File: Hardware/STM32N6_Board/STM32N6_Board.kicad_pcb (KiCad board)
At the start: 4 copper layers, 82 x 78.7 mm, 148 parts, among them J1 Conn_01x02_Pin, J10 BOOT0, J11 Conn_01x18_Socket, J12 Conn_01x18_Socket, J2 Conn_01x02_Pin, J3 Conn_01x08_Pin, J4 Conn_01x18_Pin, J5 Conn_01x18_Pin, J6 Conn_01x05_Pin, J7 SFW15R-2STE1LF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

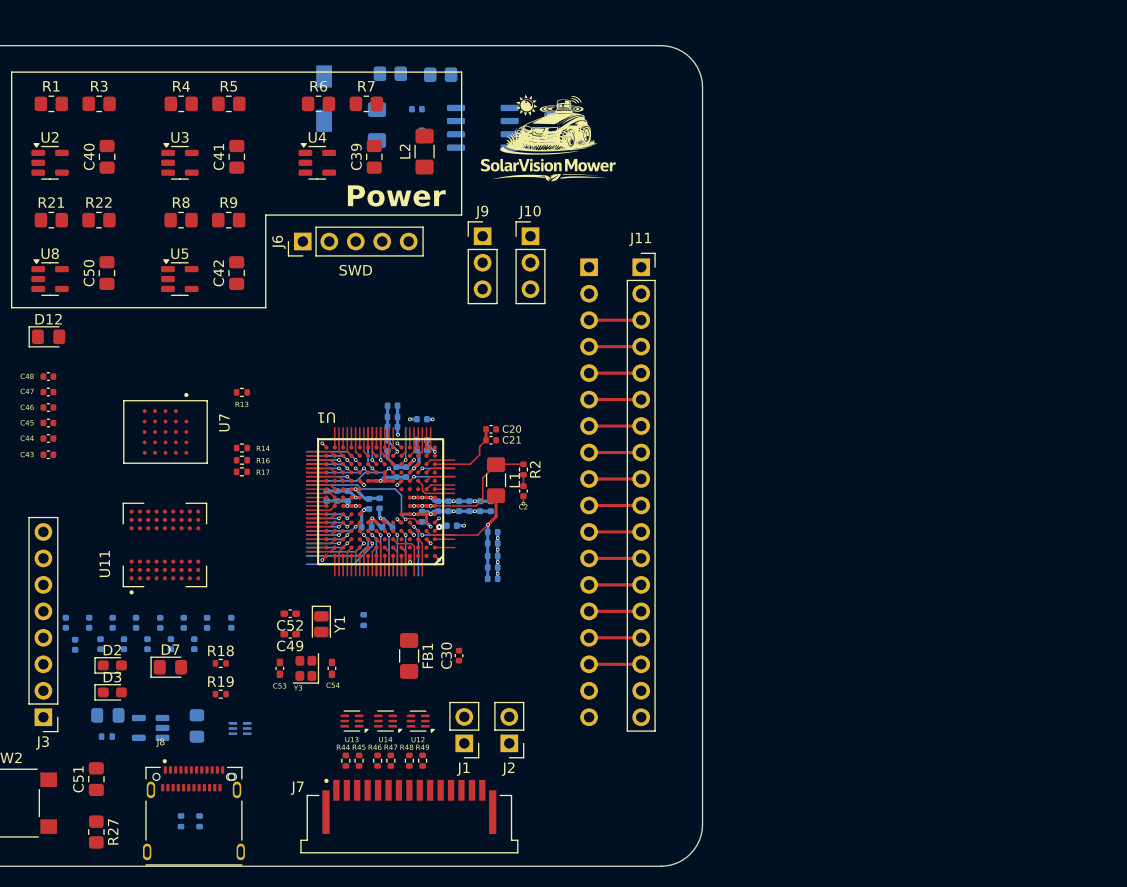
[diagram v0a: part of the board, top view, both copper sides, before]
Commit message: Finished the SDRAM wiring
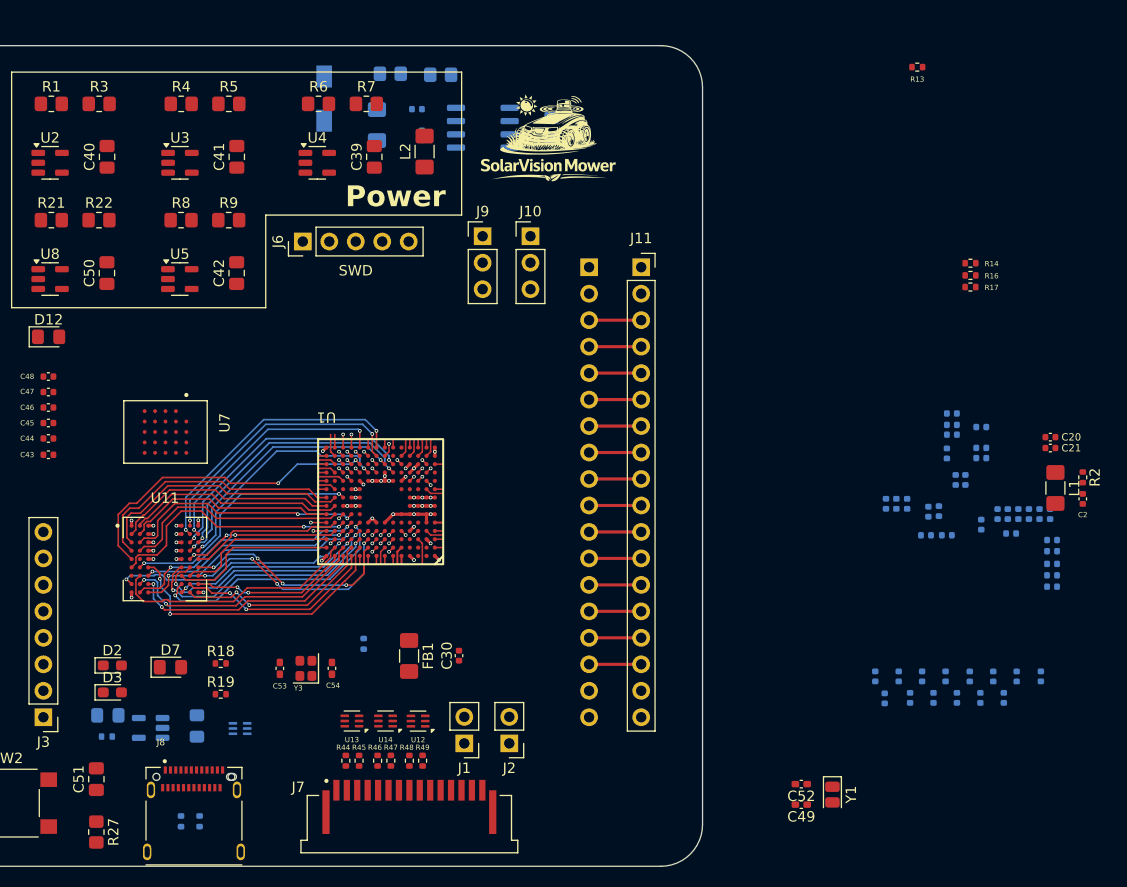
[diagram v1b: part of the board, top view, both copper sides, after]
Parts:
- moved C55 77.8 mm to (250.8, 141.3)
- moved C56 77.8 mm to (253.0, 141.3)
- moved C60 77.8 mm to (248.4, 141.4)
- moved C61 77.8 mm to (254.2, 139.3)
- moved C63 77.8 mm to (249.7, 139.3)
- moved C64 77.8 mm to (247.5, 139.3)
- moved C65 77.8 mm to (263.3, 139.3)
- moved C66 77.8 mm to (261.0, 139.3)
- moved C67 77.8 mm to (258.8, 139.3)
- moved C68 77.8 mm to (256.5, 139.3)
- moved C57 77.8 mm to (255.3, 141.3)
- moved C58 77.8 mm to (257.5, 141.3)
- moved C59 77.8 mm to (259.8, 141.3)
- moved C62 77.8 mm to (252.0, 139.3)
- moved R14 72.1 mm to (256.6, 99.6)
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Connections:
- U11 pad A2: /FMC_SDRAM/FMC_D15 -> /FMC_SDRAM/FMC_D12
- U11 pad A8: /FMC_SDRAM/FMC_D0 -> /FMC_SDRAM/FMC_D5
- U11 pad B1: /FMC_SDRAM/FMC_D14 -> /FMC_SDRAM/FMC_D13
- U11 pad B2: /FMC_SDRAM/FMC_D13 -> /FMC_SDRAM/FMC_D11
- U11 pad B8: /FMC_SDRAM/FMC_D2 -> /FMC_SDRAM/FMC_D4
- U11 pad B9: /FMC_SDRAM/FMC_D1 -> /FMC_SDRAM/FMC_D7
- U11 pad C1: /FMC_SDRAM/FMC_D12 -> /FMC_SDRAM/FMC_D15
- U11 pad C2: /FMC_SDRAM/FMC_D11 -> /FMC_SDRAM/FMC_D8
- U11 pad C8: /FMC_SDRAM/FMC_D4 -> /FMC_SDRAM/FMC_D1
- U11 pad C9: /FMC_SDRAM/FMC_D3 -> /FMC_SDRAM/FMC_D0
- U11 pad D1: /FMC_SDRAM/FMC_D10 -> /FMC_SDRAM/FMC_D14
- U11 pad D2: /FMC_SDRAM/FMC_D9 -> /FMC_SDRAM/FMC_D10
- U11 pad D8: /FMC_SDRAM/FMC_D6 -> /FMC_SDRAM/FMC_D3
- U11 pad D9: /FMC_SDRAM/FMC_D5 -> /FMC_SDRAM/FMC_D6
- U11 pad E1: /FMC_SDRAM/FMC_D8 -> /FMC_SDRAM/FMC_D9
- U11 pad E9: /FMC_SDRAM/FMC_D7 -> /FMC_SDRAM/FMC_D2
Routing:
- net GND: track 39.4 -> 13.8 mm, vias 21 -> 17
- net /FMC_SDRAM/FMC_D4: track 1.90 -> 27.1 mm, vias 0 -> 2
- net /FMC_SDRAM/FMC_D9: track 5.60 -> 30.8 mm, vias 1 -> 2
- net /FMC_SDRAM/FMC_SDCKE0: track 2.87 -> 27.6 mm, vias 0 -> 2
- net /FMC_SDRAM/FMC_D14: track 1.90 -> 25.3 mm
- net /FMC_SDRAM/FMC_D5: track 2.87 -> 25.7 mm, vias 0 -> 2
- net /FMC_SDRAM/FMC_D1: track 3.67 -> 26.4 mm, vias 0 -> 2
- net /FMC_SDRAM/FMC_D15: track 2.87 -> 24.6 mm
- net /FMC_SDRAM/FMC_D7: track 1.90 -> 23.6 mm, vias 0 -> 2
- net /FMC_SDRAM/FMC_A7: track 2.87 -> 24.2 mm, vias 0 -> 2
- net /FMC_SDRAM/FMC_D3: track 3.67 -> 25.0 mm, vias 1 -> 2
- net /FMC_SDRAM/FMC_A6: track 1.90 -> 23.1 mm, vias 0 -> 2
- net /FMC_SDRAM/FMC_NBL1: track 3.67 -> 24.7 mm, vias 1 -> 2
- net /FMC_SDRAM/FMC_A11: track 2.87 -> 23.9 mm
- net /FMC_SDRAM/FMC_SDCLK: track 3.67 -> 23.7 mm, vias 0 -> 2
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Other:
- copper layers 4 -> 6

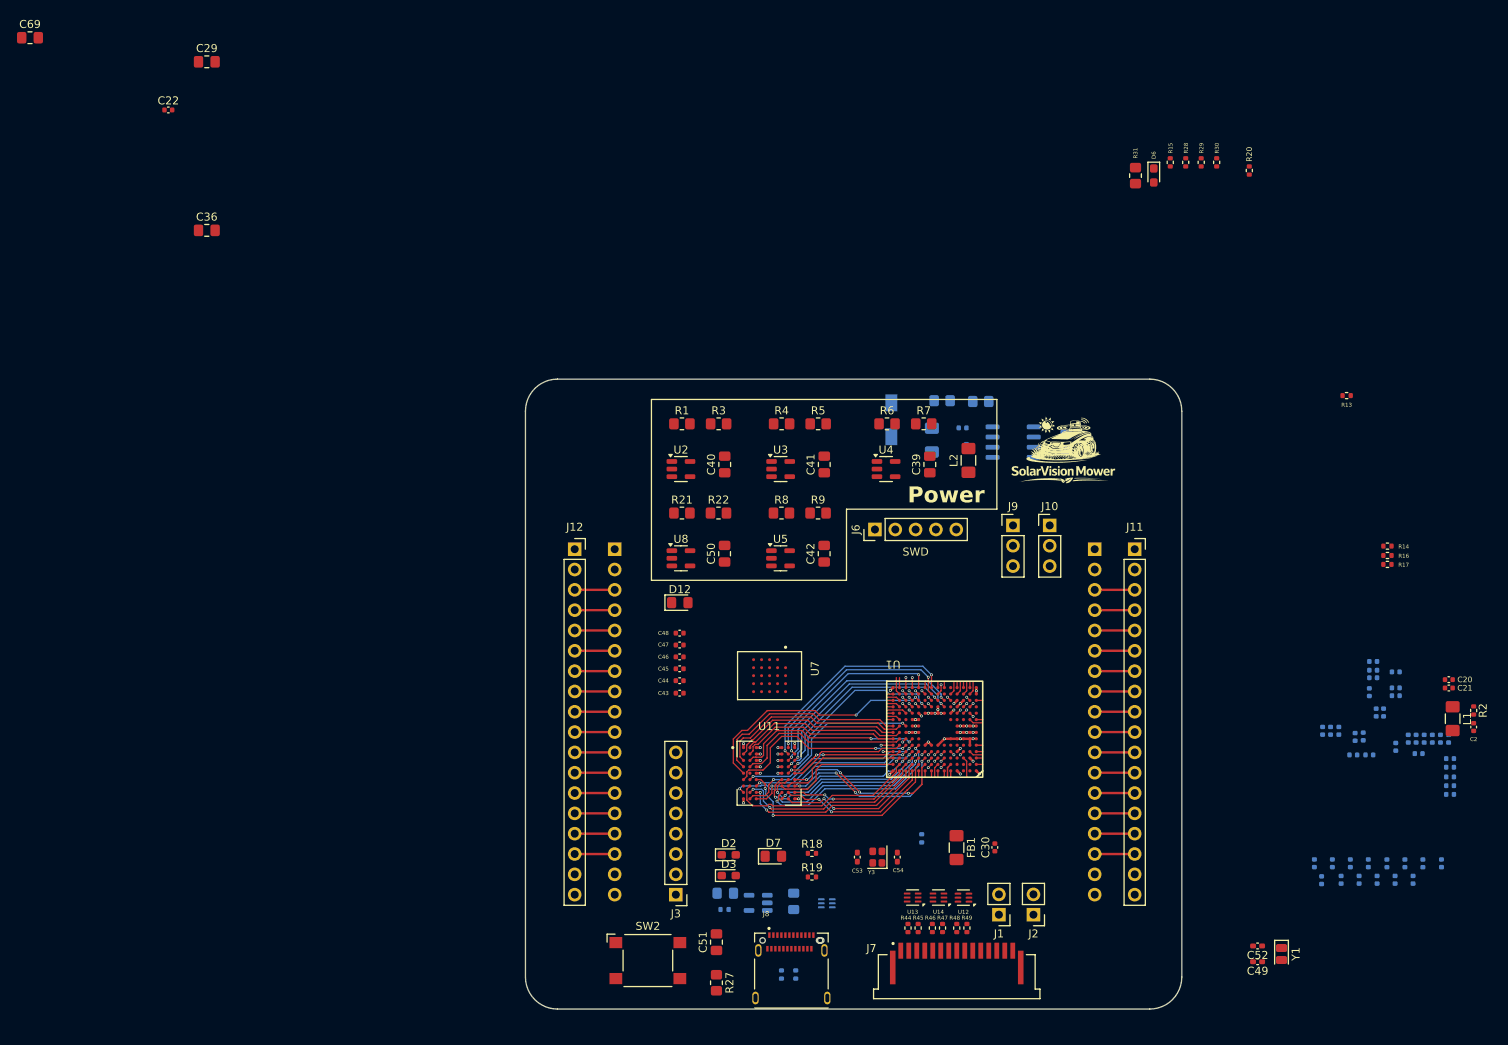
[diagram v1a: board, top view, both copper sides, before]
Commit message: added decoupling caps and other stuffs
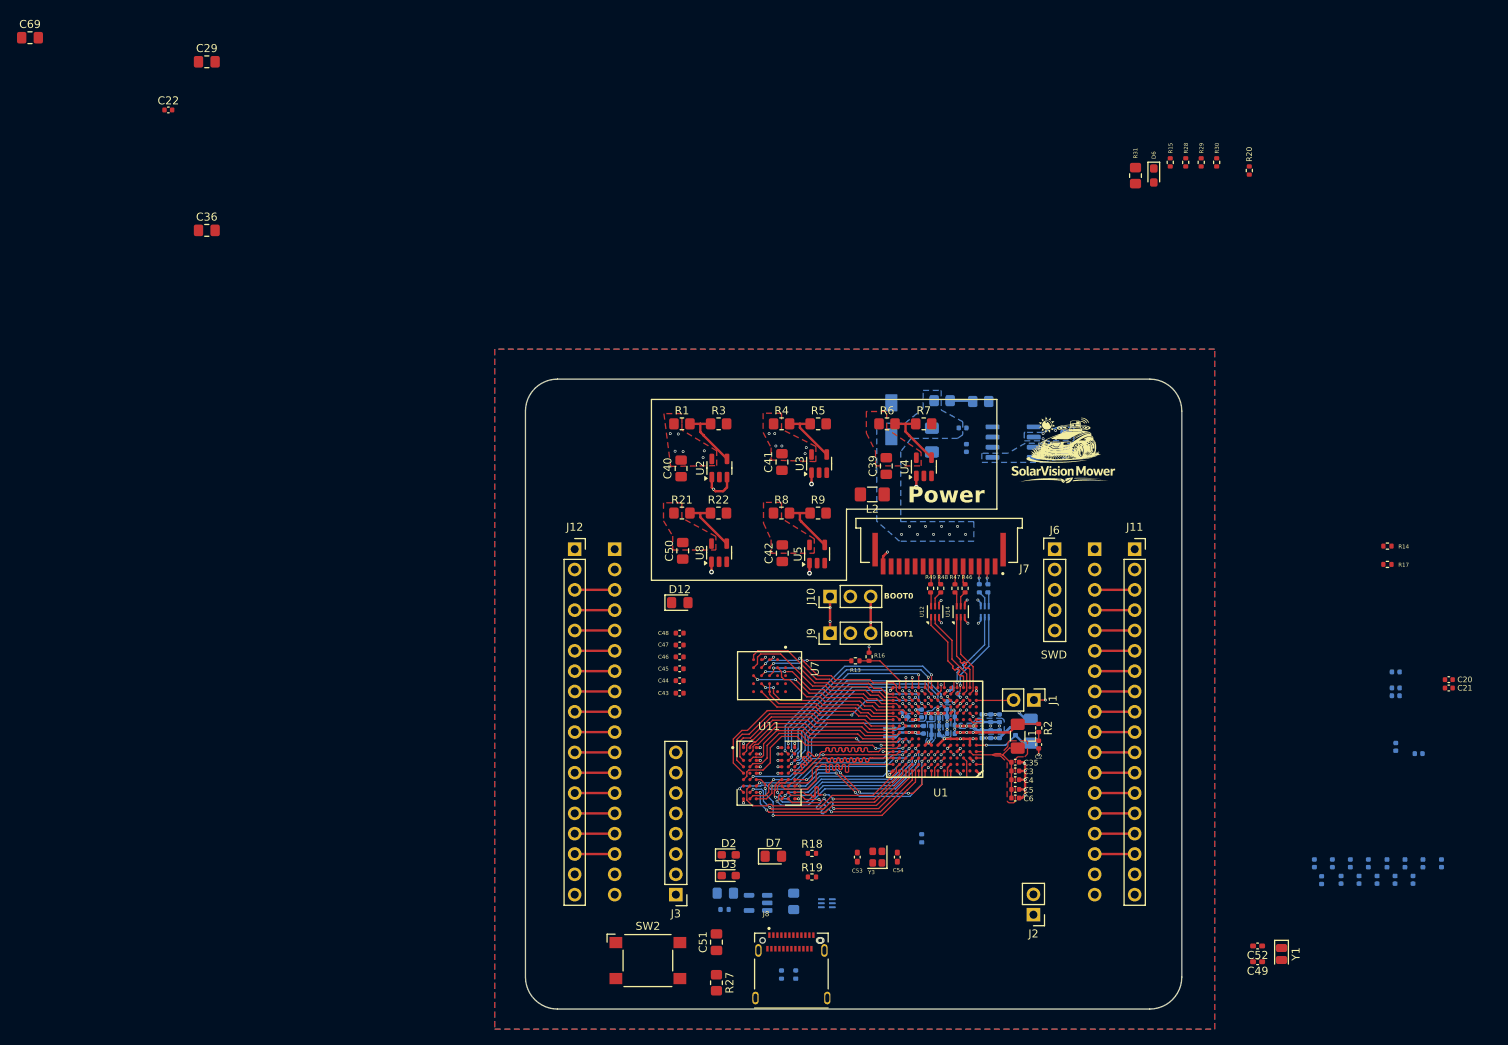
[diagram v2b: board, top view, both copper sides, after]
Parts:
- C3, C35, C4, C5, C6: moved to F.Cu
- C30, FB1, R44, R45, U13: moved to B.Cu
- moved R13 69.8 mm to (190.1, 114.0)
- moved R16 66.0 mm to (191.8, 113.4), turned to 90 degrees
- moved C12 58.3 mm to (205.9, 123.1)
- moved C11 57.4 mm to (205.9, 121.1), turned to 90 degrees
- moved C14 56.7 mm to (193.8, 122.9)
- moved C18 56.2 mm to (196.3, 120.7), turned to 135 degrees
- moved C17 56.2 mm to (198.3, 120.5), turned to 90 degrees
- moved C10 55.2 mm to (207.0, 123.1)
- moved C24 55.0 mm to (200.1, 121.1)
- moved C6 54.6 mm to (210.1, 131.1)
- moved C35 54.5 mm to (210.1, 126.6)
- moved C5 54.4 mm to (210.1, 130.0)
- moved C2 54.4 mm to (213.0, 124.4)
- moved R2 54.4 mm to (213.0, 122.3)
- moved L1 54.4 mm to (210.4, 123.4)
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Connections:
- net /Analog_Unit/D0N renamed /Analog_Unit/D0_N
- net /Analog_Unit/D0P renamed /Analog_Unit/D0_P
- net /Analog_Unit/uD0N renamed /Analog_Unit/uD0_N
- net /Analog_Unit/uD0P renamed /Analog_Unit/uD0_P
- R46 pad 1: /Analog_Unit/D1N -> /Analog_Unit/D1_N
- R47 pad 1: /Analog_Unit/D1P -> /Analog_Unit/D1_P
- R48 pad 1: /Analog_Unit/CKN -> /Analog_Unit/CK_N
- R49 pad 1: /Analog_Unit/CKP -> /Analog_Unit/CK_P
- U1 pad N2: /Analog_Unit/uD1N -> /Analog_Unit/uD1_N
- U1 pad N3: /Analog_Unit/uCKN -> /Analog_Unit/uCK_N
- U1 pad P2: /Analog_Unit/uD1P -> /Analog_Unit/uD1_P
- U1 pad P3: /Analog_Unit/uCKP -> /Analog_Unit/uCK_P
- U12 pad 1: /Analog_Unit/uCKN -> /Analog_Unit/uCK_P
- U12 pad 2: /Analog_Unit/uCKP -> /Analog_Unit/uCK_N
- U12 pad 5: /Analog_Unit/CKP -> /Analog_Unit/CK_N
- U12 pad 6: /Analog_Unit/CKN -> /Analog_Unit/CK_P
- U14 pad 1: /Analog_Unit/uD1N -> /Analog_Unit/uD1_P
- U14 pad 2: /Analog_Unit/uD1P -> /Analog_Unit/uD1_N
- U14 pad 5: /Analog_Unit/D1P -> /Analog_Unit/D1_N
- U14 pad 6: /Analog_Unit/D1N -> /Analog_Unit/D1_P
- U7 pad C5: unconnected-(U7-NC-PadC5) -> /GPIO/PN4
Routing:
- net GND: track 13.8 -> 53.7 mm, vias 17 -> 41
- net /GPIO/PN10: track 0.80 -> 21.0 mm
- net /GPIO/PN11: track 0.80 -> 20.5 mm
- net /GPIO/PN9: track 0.80 -> 19.1 mm, vias 0 -> 2
- net /GPIO/PN3: track 2.22 -> 20.0 mm, vias 0 -> 2
- net /GPIO/PN5: track 0.80 -> 18.4 mm, vias 0 -> 2
- net /GPIO/PN2: track 1.77 -> 19.3 mm, vias 0 -> 2
- net /GPIO/PN4: track 1.77 -> 18.9 mm
- net /GPIO/PN8: track 0.85 -> 17.9 mm
- net /GPIO/PN0: track 1.77 -> 18.6 mm, vias 0 -> 2
- net /GPIO/PN6: track 2.57 -> 18.8 mm
- net VDD: track 4.10 -> 17.9 mm, vias 5 -> 18
- net /Analog_Unit/uCK_N: track 0.00 -> 11.4 mm
- net /Analog_Unit/uCK_P: track 0.00 -> 11.4 mm
- net /Power_Unit/VFBSMPS: track 1.77 -> 12.4 mm
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- added copper zone on B.Cu, net +5V
- added copper zone on B.Cu, net /Power_Unit/Buck_Feedback
- added copper zone on B.Cu, net /Power_Unit/VDDCORE
- added copper zone on B.Cu, net /Power_Unit/VDDSMPS
- added copper zone on F.Cu, net /Power_Unit/VFBSMPS
- added copper zone on F.Cu, net /XSPI NOR Flash/VDD_OCTO
- added copper zone on B.Cu, net GND
- added copper zone on F.Cu, net GND
- added copper zone on In4.Cu, net GND
- added copper zone on B.Cu, net VDD
- added copper zone on In2.Cu, net VDD
- added copper zone on F.Cu, net VDD1V8
- added copper zone on F.Cu, net VDD3V3
- added copper zone on F.Cu, net VDDA1V8
- added copper zone on F.Cu, net VDDA1V8_AON
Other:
- board text added: "BOOT0"
- board text added: "BOOT1"

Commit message: almost finished with the board
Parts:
- removed C2: 2.2n, Capacitor_SMD:C_0402_1005Metric
- removed C6: 15u, Capacitor_SMD:C_0402_1005Metric
- removed J2: Conn_01x02_Pin, Connector_PinHeader_2.54mm:PinHeader_1x02_P2.54mm_Vertical
- removed J8: 12401832E402A, STM32N6_Footprints:AMPHENOL_12401832E402A
- removed L1: 1u, Inductor_SMD:L_1206_3216Metric_Pad1.42x1.75mm_HandSolder
- removed R2: 2, Resistor_SMD:R_0402_1005Metric
- added D10: D_TVS, LED_SMD:LED_0805_2012Metric_Pad1.15x1.40mm_HandSolder, F.Cu at (222.6, 146.4)
- added D8: D_TVS, LED_SMD:LED_0805_2012Metric_Pad1.15x1.40mm_HandSolder, F.Cu at (157.7, 146.4)
- added D9: D_TVS, LED_SMD:LED_0805_2012Metric_Pad1.15x1.40mm_HandSolder, F.Cu at (222.4, 95.2)
- added FB2: 70R@100M, Inductor_SMD:L_1206_3216Metric_Pad1.42x1.75mm_HandSolder, F.Cu at (210.6, 123.7)
- added J13: TYPE-C_16PIN_2MD__073_, STM32N6_Footprints:SHOUHAN_TYPE-C_16PIN_2MD__073_, F.Cu at (190.2, 154.6)
- added REF**: MountingHole_2.5mm_Pad, MountingHole:MountingHole_2.5mm_Pad, F.Cu at (226.9, 153.5)
- added REF**: MountingHole_2.5mm_Pad, MountingHole:MountingHole_2.5mm_Pad, F.Cu at (152.8, 82.7)
- added REF**: MountingHole_2.5mm_Pad, MountingHole:MountingHole_2.5mm_Pad, F.Cu at (226.9, 82.7)
- added REF**: MountingHole_2.5mm_Pad, MountingHole:MountingHole_2.5mm_Pad, F.Cu at (152.8, 153.5)
- C1, C32, C56, C57, D4, D5, R26, U10, U9: moved to F.Cu
- C20, C21, C22, C29, C43, C44, C45, C46, C47, C48, C49, C52, C69, L2, R14, R17, R19, Y1: moved to B.Cu
- R31: footprint Resistor_SMD:R_0805_2012Metric_Pad1.20x1.40mm_HandSolder -> Resistor_SMD:R_0402_1005Metric
- moved C22 132.7 mm to (206.8, 129.2)
- moved C29 128.0 mm to (199.7, 129.4), turned to -90 degrees
- moved C69 126.2 mm to (199.0, 94.2)
- moved R28 104.9 mm to (158.2, 126.7), turned to 180 degrees
- moved R15 101.7 mm to (158.2, 124.2), turned to 180 degrees
- moved C65 87.3 mm to (176.9, 127.2), turned to 180 degrees
- moved C66 84.9 mm to (176.9, 128.2), turned to 180 degrees
- moved C59 82.7 mm to (179.4, 122.0), turned to 90 degrees
- moved C67 80.6 mm to (179.3, 125.8), turned to 180 degrees
- moved C58 79.4 mm to (180.5, 122.0), turned to 90 degrees
- moved C68 78.2 mm to (179.3, 126.8), turned to 180 degrees
- moved R17 76.9 mm to (181.6, 119.0), turned to 180 degrees
- moved C61 76.5 mm to (179.3, 123.8), turned to 180 degrees
- moved R30 76.3 mm to (221.9, 126.7), turned to 0 degrees
- moved R14 76.1 mm to (182.6, 117.4), turned to -90 degrees
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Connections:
- net VBUS_A renamed /Analog_Unit/VBUS
- C3 pad 1: /Power_Unit/VFBSMPS -> /Power_Unit/VDDCORE
- C35 pad 1: /Power_Unit/VFBSMPS -> /Power_Unit/VDDCORE
- C4 pad 1: /Power_Unit/VFBSMPS -> /Power_Unit/VDDCORE
- C5 pad 1: /Power_Unit/VFBSMPS -> /Power_Unit/VDDCORE
- D7 pad 1: +5V -> GND
- D7 pad 2: GND -> +5V
- J11 pad 13: /Connectors/TIM2_CH1 -> /Connectors/TIM1_CH4
- J11 pad 15: /Connectors/TIM4_CH1 -> /Connectors/TIM3_CH3
- J12 pad 14: /Connectors/TIM1_CH4 -> /Connectors/TIM2_CH1
- J12 pad 16: /Connectors/TIM3_CH3 -> /Connectors/TIM4_CH1
- J4 pad 13: /Connectors/TIM2_CH1 -> /Connectors/TIM1_CH4
- J4 pad 15: /Connectors/TIM4_CH1 -> /Connectors/TIM3_CH3
- J5 pad 14: /Connectors/TIM1_CH4 -> /Connectors/TIM2_CH1
- J5 pad 16: /Connectors/TIM3_CH3 -> /Connectors/TIM4_CH1
- J7 pad 13: /Connectors/I2C1_SCL -> /Connectors/I2C2_SCL
- J7 pad 14: /Connectors/I2C1_SDA -> /Connectors/I2C2_SDA
- R14 pad 2: /XSPI NOR Flash/VDD_OCTO -> VDD
- R16 pad 2: /XSPI NOR Flash/VDD_OCTO -> VDD
- R17 pad 2: /XSPI NOR Flash/VDD_OCTO -> VDD
- R26 pad 2: /Analog_Unit/EN -> /Analog_Unit/EN_USB
- U1 pad A5: /Analog_Unit/uHSDM -> /Analog_Unit/uHSD_N
- U1 pad B5: /Analog_Unit/uHSDP -> /Analog_Unit/uHSD_P
- U1 pad D2: /Power_Unit/VFBSMPS -> /Power_Unit/VDDCORE
- U10 pad 4: /Analog_Unit/EN -> /Analog_Unit/EN_USB
- U9 pad 1: /Analog_Unit/HSDP -> /Analog_Unit/HSD_N
- U9 pad 2: /Analog_Unit/HSDM -> /Analog_Unit/HSD_P
- U9 pad 5: /Analog_Unit/uHSDM -> /Analog_Unit/uHSD_P
- U9 pad 6: /Analog_Unit/uHSDP -> /Analog_Unit/uHSD_N
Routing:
- net VDDA1V8: track 3.15 -> 148.5 mm, vias 9 -> 12
- net /Analog_Unit/NRST: track 0.00 -> 129.3 mm, vias 0 -> 5
- net /Analog_Unit/PWR_ON: track 0.00 -> 96.0 mm, vias 0 -> 4
- net /Analog_Unit/FAULT: track 0.57 -> 78.3 mm, vias 1 -> 7
- net /Analog_Unit/EN_USB: track 0.57 -> 77.2 mm, vias 1 -> 6
- net /Connectors/SPI1_NSS: track 5.80 -> 77.9 mm, vias 0 -> 2
- net VDD1V8: track 1.79 -> 69.6 mm, vias 1 -> 6
- net /Connectors/TIM1_CH3: track 6.32 -> 72.1 mm
- net /Connectors/I2C2_SDA: track 5.57 -> 70.7 mm, vias 1 -> 3
- net /Connectors/TIM4_CH1: track 5.80 -> 68.9 mm, vias 0 -> 3
- net /Connectors/I2C2_SCL: track 6.25 -> 68.8 mm, vias 1 -> 3
- net /Analog_Unit/BOOT0: track 0.57 -> 56.9 mm, vias 1 -> 2
- net /Connectors/I2C1_SCL: track 5.57 -> 60.0 mm, vias 1 -> 2
- net /Connectors/SPI1_MISO: track 5.57 -> 59.2 mm, vias 1 -> 2
- net /Connectors/SPI1_MOSI: track 5.57 -> 59.0 mm, vias 1 -> 2
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- added copper zone on F.Cu, net +5V
- added copper zone on F.Cu, net /Analog_Unit/VBUS
- added copper zone on In2.Cu, net /Analog_Unit/VBUS
- added copper zone on F.Cu, net /Power_Unit/VDDCORE
- added copper zone on In2.Cu, net /Power_Unit/VDDSMPS
- added copper zone on B.Cu, net /Power_Unit/VREFP
- added copper zone on In2.Cu, net /XSPI NOR Flash/VDD_OCTO
- added copper zone on In3.Cu, net GND
- added copper zone on In2.Cu, net VDD3V3
- added copper zone on In2.Cu, net VDDA1V8_AON
- removed copper zone on F.Cu, net /Power_Unit/VFBSMPS
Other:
- board text added: "VDD BOOT GND"
- board text added: "VREFP-1V8"
